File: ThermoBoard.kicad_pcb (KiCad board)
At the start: 4 copper layers, 97 x 97 mm, 139 parts, among them J100 Conn_01x05_Pin, J101 Screw_Terminal_01x02, J102 USB_C_Receptacle_USB2.0_16P, J200 RJ45_Hanrun_HR911105A_Horizon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, J300 PCC-SMP-K-5, J301 PCC-SMP-K-5, J302 PCC-SMP-K-5, J303 PCC-SMP-K-5, J400 Conn_01x03, Q100 Si2371EDS, SW100 SKRPANE010, U100 STM32H563RITx, U101 AP2112K-3.3, U102 USBLC6-2SC6, U200 LAN8742A, U300 MAX31856, U301 MAX31856, U302 MAX31856, U303 MAX31856, U400 TJA1042T-3, Y100 16MHz, Y200 25MHz

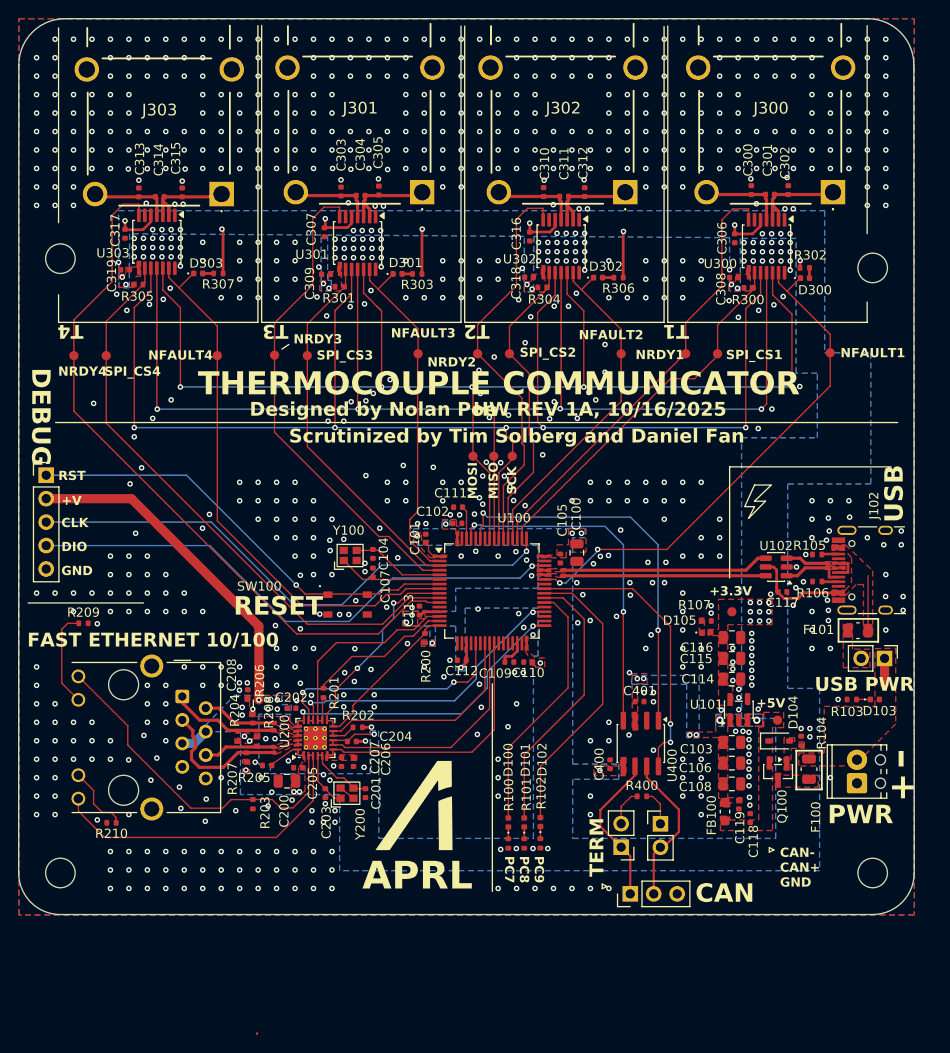
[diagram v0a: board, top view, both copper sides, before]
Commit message: Rev 1B - Fix silkscreen, board outline, ethernet pinout
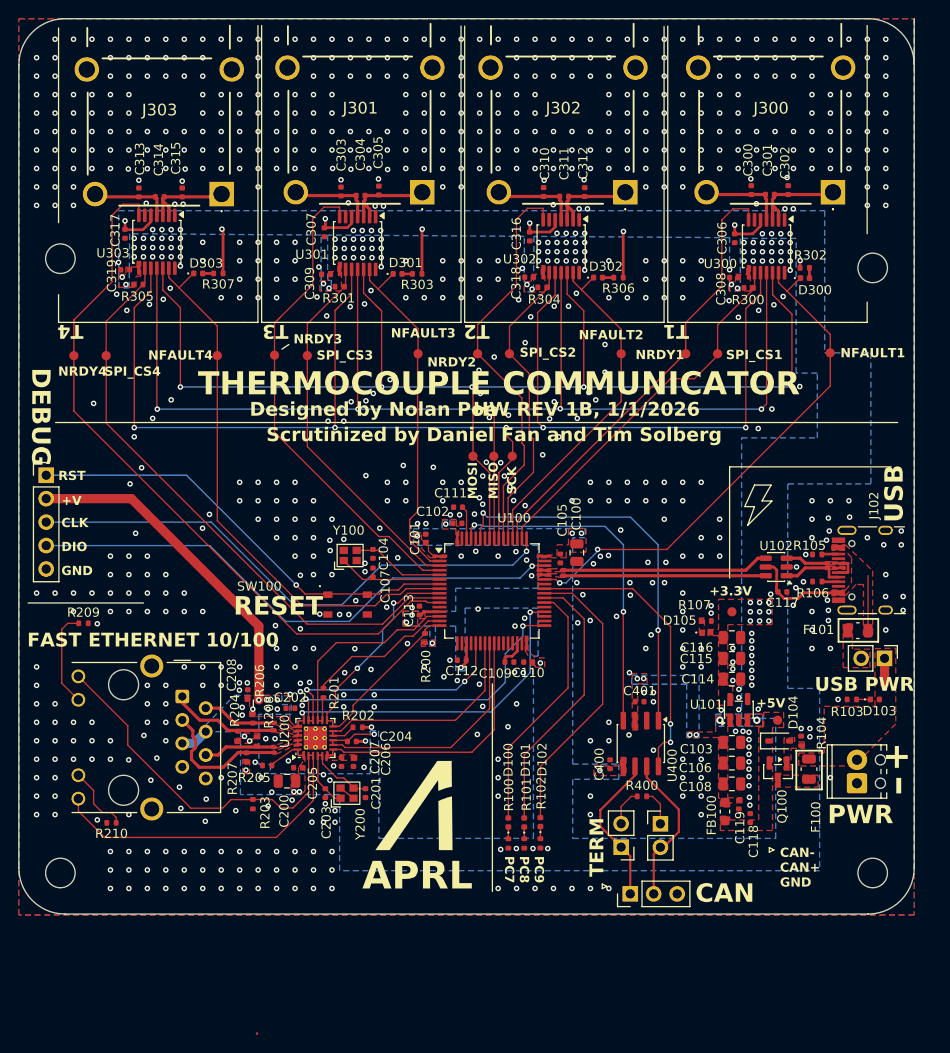
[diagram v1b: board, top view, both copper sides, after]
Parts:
- moved C202 0.11 mm to (119.9, 131.4)
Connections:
- U200 pad 16: ETH_TXD1 -> ETH_TX_EN
- U200 pad 17: ETH_TX_EN -> ETH_TXD0
- U200 pad 18: ETH_TXD0 -> ETH_TXD1
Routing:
- net ETH_TXD1: track 32.2 -> 35.5 mm
- net ETH_TXD0: track 32.2 -> 34.0 mm
- net ETH_TX_EN: track 26.2 -> 25.7 mm
- net GND: vias 930 -> 932
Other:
- outline, holes or cut-outs redrawn
- board text added: "HW REV 1B, 1/1/2026"
- board text added: "Scrutinized by Daniel Fan and Tim Solberg"
- board text removed: "HW REV 1A, 10/16/2025"
- board text removed: "Scrutinized by Tim Solberg and Daniel Fan"
